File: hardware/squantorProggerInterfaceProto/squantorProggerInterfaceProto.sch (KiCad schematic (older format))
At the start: 24 parts, among them J1 JTAG_interface_proto_input, J2 JTAG_interface_proto_output, U1 74X1T45, U2 74X1T45, U3 74X1T45, U4 74X1T45, U5 74X1G125

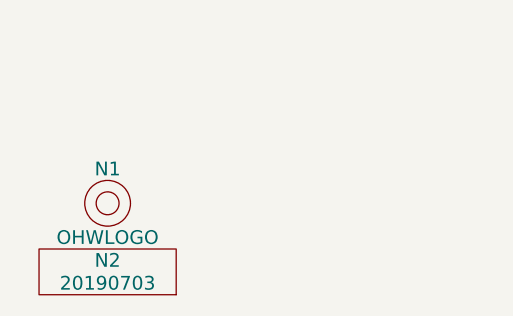
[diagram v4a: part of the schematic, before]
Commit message: changed OSH logo, front silk mistake fixed
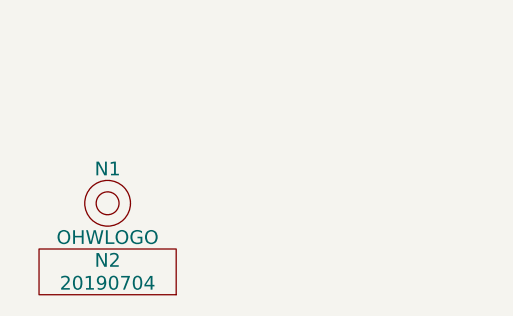
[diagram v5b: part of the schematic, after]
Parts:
- J1: footprint SquantorConnectors:Header-0254-1X08-H010 -> SquantorConnectorsNamed:JTAG-interface-proto-input
- J2: footprint SquantorConnectors:Header-0254-1X08-H010 -> SquantorConnectorsNamed:JTAG-interface-proto-output
- N1: footprint Symbols:OSHW-Symbol_6.7x6mm_SilkScreen -> Symbol:OSHW-Logo_5.7x6mm_SilkScreen
- N2: value 20190703 -> 20190704
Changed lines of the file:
@@
 P 850 7700
 F 0 "N2" H 850 7800 60  0000 C CNN
-F 1 "20190703" H 850 7700 60  0000 C CNN
+F 1 "20190704" H 850 7700 60  0000 C CNN
 F 2 "SquantorLabels:Label_version" H 850 7700 60  0001 C CNN
 F 3 "" H 850 7700 60  0001 C CNN
@@
 F 0 "N1" H 850 7500 60  0000 C CNN
 F 1 "OHWLOGO" H 850 7200 60  0000 C CNN
-F 2 "Symbols:OSHW-Symbol_6.7x6mm_SilkScreen" H 850 7350 60  0001 C CNN
+F 2 "Symbol:OSHW-Logo_5.7x6mm_SilkScreen" H 850 7350 60  0001 C CNN
 F 3 "" H 850 7350 60  0001 C CNN
 	1    850  7350
@@
 F 0 "J1" H 1083 2215 50  0000 C CNN
 F 1 "JTAG_interface_proto_input" H 1083 2124 50  0000 C CNN
-F 2 "SquantorConnectors:Header-0254-1X08-H010" H 1100 1400 50  0001 C CNN
+F 2 "SquantorConnectorsNamed:JTAG-interface-proto-input" H 1100 1400 50  0001 C CNN
 F 3 "" H 1100 1400 50  0001 C CNN
 	1    1050 1400
@@
 F 0 "J2" H 2682 1046 50  0000 R CNN
 F 1 "JTAG_interface_proto_output" H 2682 955 50  0000 R CNN
-F 2 "SquantorConnectors:Header-0254-1X08-H010" H 3000 1100 50  0001 C CNN
+F 2 "SquantorConnectorsNamed:JTAG-interface-proto-output" H 3000 1100 50  0001 C CNN
 F 3 "" H 3000 1100 50  0001 C CNN
 	1    3000 1100

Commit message: final checks, in production
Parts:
- N2: value 20190704 -> 20190705
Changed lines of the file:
@@
 P 850 7700
 F 0 "N2" H 850 7800 60  0000 C CNN
-F 1 "20190704" H 850 7700 60  0000 C CNN
+F 1 "20190705" H 850 7700 60  0000 C CNN
 F 2 "SquantorLabels:Label_version" H 850 7700 60  0001 C CNN
 F 3 "" H 850 7700 60  0001 C CNN
